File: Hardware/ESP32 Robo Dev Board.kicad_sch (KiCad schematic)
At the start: 19 parts, among them J1 PRG, U1 ESP32-S3-WROOM-1, U2 AMS1117-3.3, U5 TCA9548ARGER

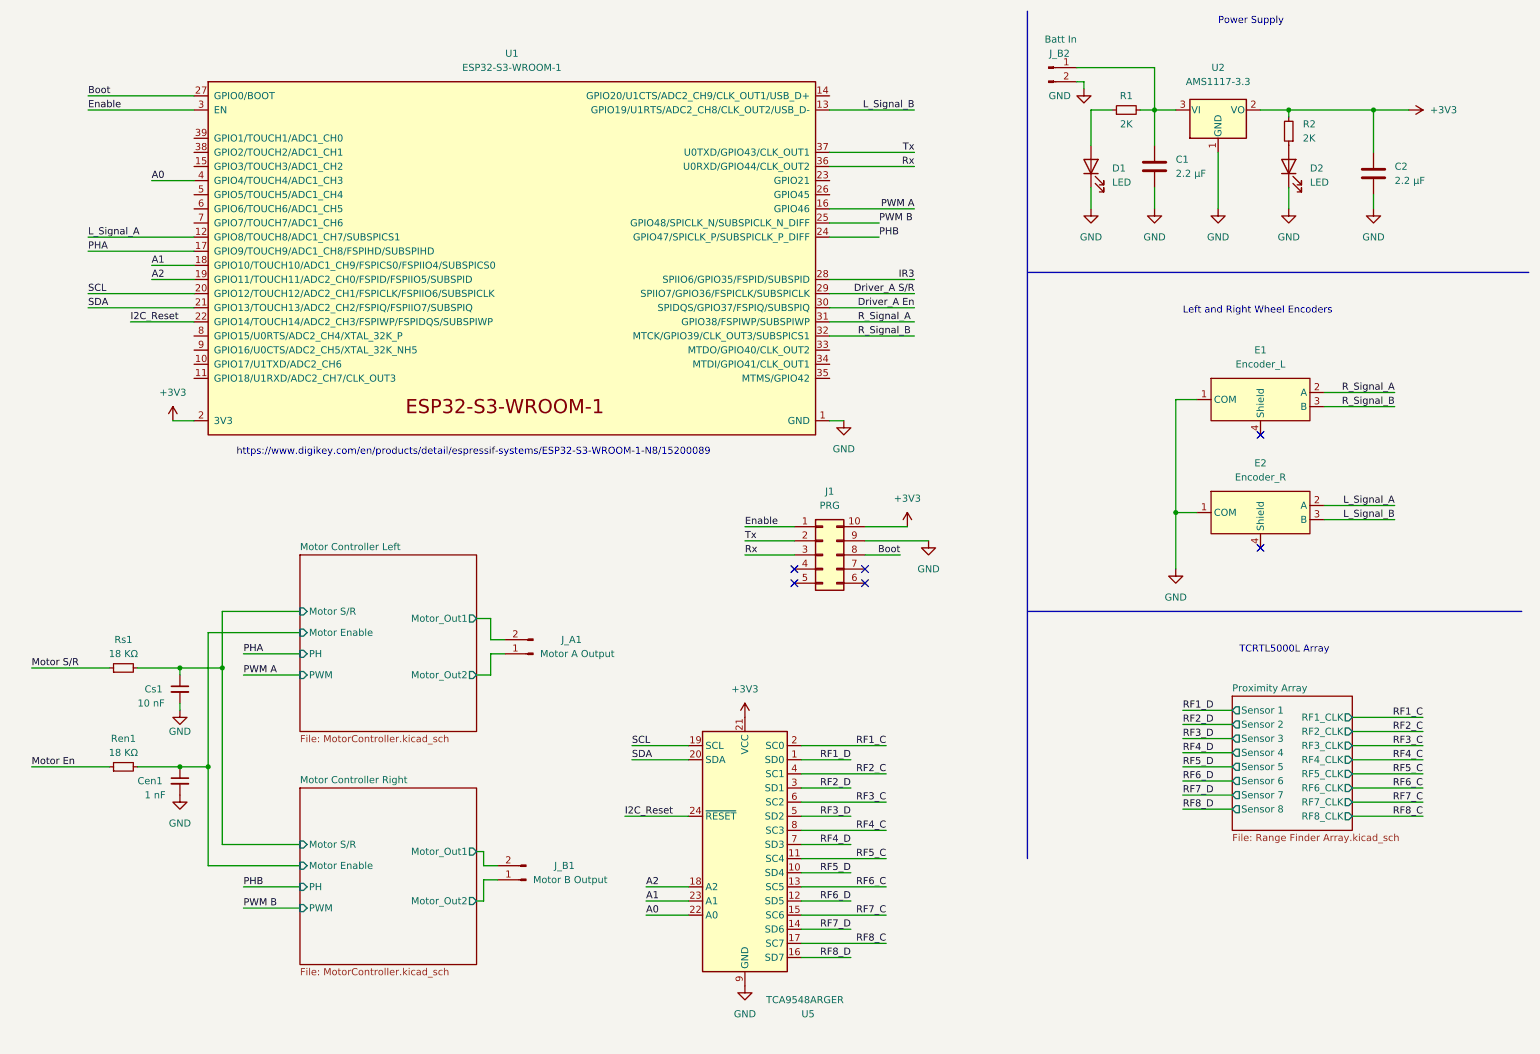
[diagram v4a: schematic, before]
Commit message: I2C Interface Established
Run Traces for all Sensors

Mark unused Pins

Sub-Optimally run said traces
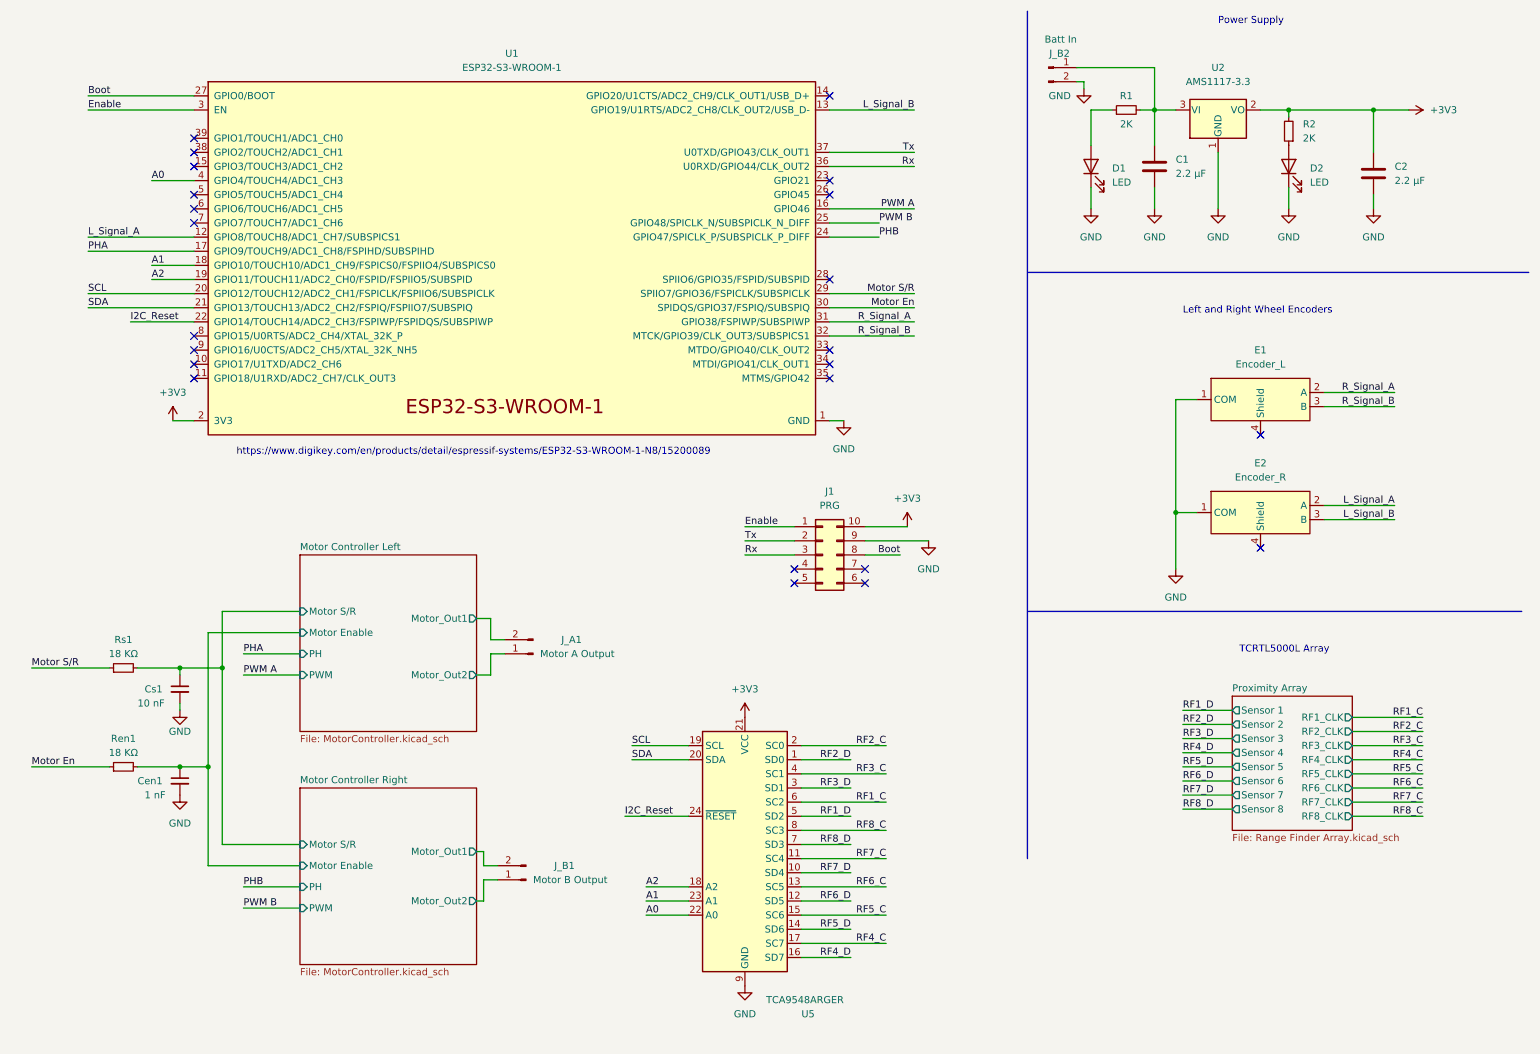
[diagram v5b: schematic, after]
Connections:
- net Driver_A En is gone; now on net Motor En: U1.30 (SPIDQS/GPIO37/FSPIQ/SUBSPIQ)
- net Driver_A S/R is gone; now on net Motor S/R: U1.29 (SPIIO7/GPIO36/FSPICLK/SUBSPICLK)
- net RF1_C: now also U5.6 (SC2); no longer U5.2 (SC0)
- net RF1_D: now also U5.5 (SD2); no longer U5.1 (SD0)
- net RF2_C: now also U5.2 (SC0); no longer U5.4 (SC1)
- net RF2_D: now also U5.1 (SD0); no longer U5.3 (SD1)
- net RF3_C: now also U5.4 (SC1); no longer U5.6 (SC2)
- net RF3_D: now also U5.3 (SD1); no longer U5.5 (SD2)
- net RF4_C: now also U5.17 (SC7); no longer U5.8 (SC3)
- net RF4_D: now also U5.16 (SD7); no longer U5.7 (SD3)
- net RF5_C: now also U5.15 (SC6); no longer U5.11 (SC4)
- net RF5_D: now also U5.14 (SD6); no longer U5.10 (SD4)
- net RF7_C: now also U5.11 (SC4); no longer U5.15 (SC6)
- net RF7_D: now also U5.10 (SD4); no longer U5.14 (SD6)
- net RF8_C: now also U5.8 (SC3); no longer U5.17 (SC7)
- net RF8_D: now also U5.7 (SD3); no longer U5.16 (SD7)
- net IR3: no longer names the net of U1.28 (SPIIO6/GPIO35/FSPID/SUBSPID)
- no-connect marks 6 -> 23

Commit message: Fix Thoughholes
Fixed Schematic Parity DRC issue.

Taught some standard practices by the Foxy Boy

Co-Authored-By: KenwoodFox <31870999+KenwoodFox@users.noreply.github.com>
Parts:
- added H1: (no value), symbol Mechanical:MountingHole_Pad
- added H2, H3, H4: MountingHole_Pad, MountingHole:MountingHole_2.2mm_M2_DIN965_Pad, symbol Mechanical:MountingHole_Pad
- renumbered U5 to U2, U2 to U3
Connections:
- net GND: now also H1.1, H2.1, H3.1, H4.1

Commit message: Add Throughholes
Added Through holes in a far better what than before.

Got advice from the Foxy Fellow

Co-Authored-By: KenwoodFox <31870999+KenwoodFox@users.noreply.github.com>
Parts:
- H1: value (none) -> MountingHole_Pad; footprint (none) -> MountingHole:MountingHole_2.2mm_M2_DIN965_Pad
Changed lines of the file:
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@@
     (title "TurtleBot Mainboard")
     (date "2022-11-27")
-    (rev "0.1")
+    (rev "${REVISION}")
     (company "Amoskeag Technologies")
+    (comment 4 "${FULL_REVISION}")
   )
   (junction (at 43.18 148.59) (diameter 0) (color 0 0 0 0)
@@
       (effects (font (size 1.27 1.27)) (justify left))
     )
-    (property "Value" "" (id 1) (at 17.78 189.2299 0)
+    (property "Value" "MountingHole_Pad" (id 1) (at 17.78 189.2299 0)
       (effects (font (size 1.27 1.27)) (justify left) hide)
     )
-    (property "Footprint" "" (id 2) (at 15.24 189.23 0)
+    (property "Footprint" "MountingHole:MountingHole_2.2mm_M2_DIN965_Pad" (id 2) (at 15.24 189.23 0)
       (effects (font (size 1.27 1.27)) hide)
     )
@@
   (symbol (lib_id "Graphic:Logo_Open_Hardware_Small") (at 261.62 175.26 0) (unit 1)
     (in_bom yes) (on_board yes) (fields_autoplaced)
-    (property "Reference" "#LOGO?" (id 0) (at 261.62 168.275 0)
-      (effects (font (size 1.27 1.27)) hide)
-    )
-    (property "Value" "" (id 1) (at 261.62 180.975 0)
-      (effects (font (size 1.27 1.27)) hide)
-    )
-    (property "Footprint" "" (id 2) (at 261.62 175.26 0)
+    (property "Reference" "#LOGO1" (id 0) (at 261.62 168.275 0)
+      (effects (font (size 1.27 1.27)) hide)
+    )
+    (property "Value" "Logo_Open_Hardware_Small" (id 1) (at 261.62 180.975 0)
+      (effects (font (size 1.27 1.27)) hide)
+    )
+    (property "Footprint" "Symbol:OSHW-Logo2_7.3x6mm_SilkScreen" (id 2) (at 261.62 175.26 0)
       (effects (font (size 1.27 1.27)) hide)
     )
@@
   (symbol (lib_id "Amoskeag-KiCAD-Lib:AT_Logo") (at 276.86 175.26 0) (unit 1)
     (in_bom yes) (on_board yes) (fields_autoplaced)
-    (property "Reference" "#G?" (id 0) (at 276.86 170.8713 0)
-      (effects (font (size 1.27 1.27)) hide)
-    )
-    (property "Value" "" (id 1) (at 276.86 179.6487 0)
+    (property "Reference" "#G1" (id 0) (at 276.86 170.8713 0)
+      (effects (font (size 1.27 1.27)) hide)
+    )
+    (property "Value" "AT_Logo" (id 1) (at 276.86 179.6487 0)
       (effects (font (size 1.27 1.27)) hide)
     )
@@
       (effects (font (size 1.27 1.27)) hide)
     )
-    (property "Value" "" (id 1) (at 15.24 196.85 0))
+    (property "Value" "GND" (id 1) (at 15.24 196.85 0))
     (property "Footprint" "" (id 2) (at 15.24 193.04 0)
       (effects (font (size 1.27 1.27)) hide)
@@
   (symbol_instances
     (path "/bc5273c3-012f-45b1-962a-d2f6bccb6a9a"
-      (reference "#G?") (unit 1) (value "AT_Logo") (footprint "")
+      (reference "#G1") (unit 1) (value "AT_Logo") (footprint "")
     )
     (path "/bbe411a0-2e88-4725-b110-84205d860b3c"
-      (reference "#LOGO?") (unit 1) (value "Logo_Open_Hardware_Small") (footprint "Symbol:OSHW-Logo2_7.3x6mm_SilkScreen")
+      (reference "#LOGO1") (unit 1) (value "Logo_Open_Hardware_Small") (footprint "Symbol:OSHW-Logo2_7.3x6mm_SilkScreen")
     )
     (path "/efc531b6-9e3c-46d2-a03c-acf3a17dc1eb"

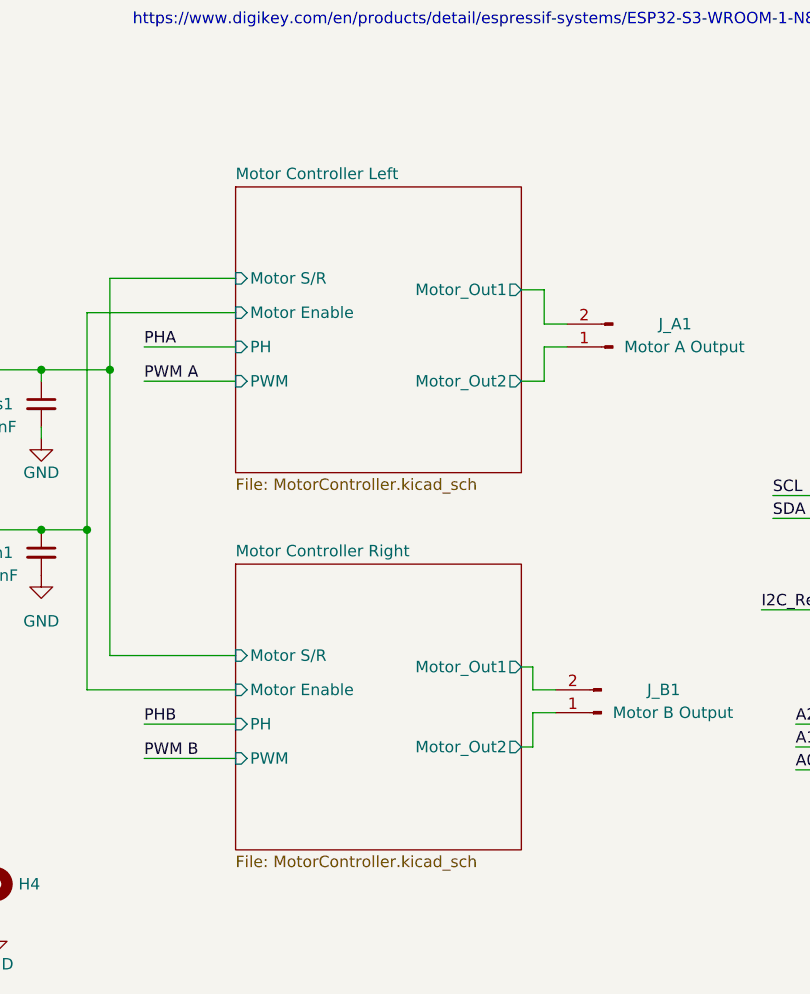
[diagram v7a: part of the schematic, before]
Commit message: Fixed Traces
Fix Traces that I messed up when I left college. Getting back to the project.
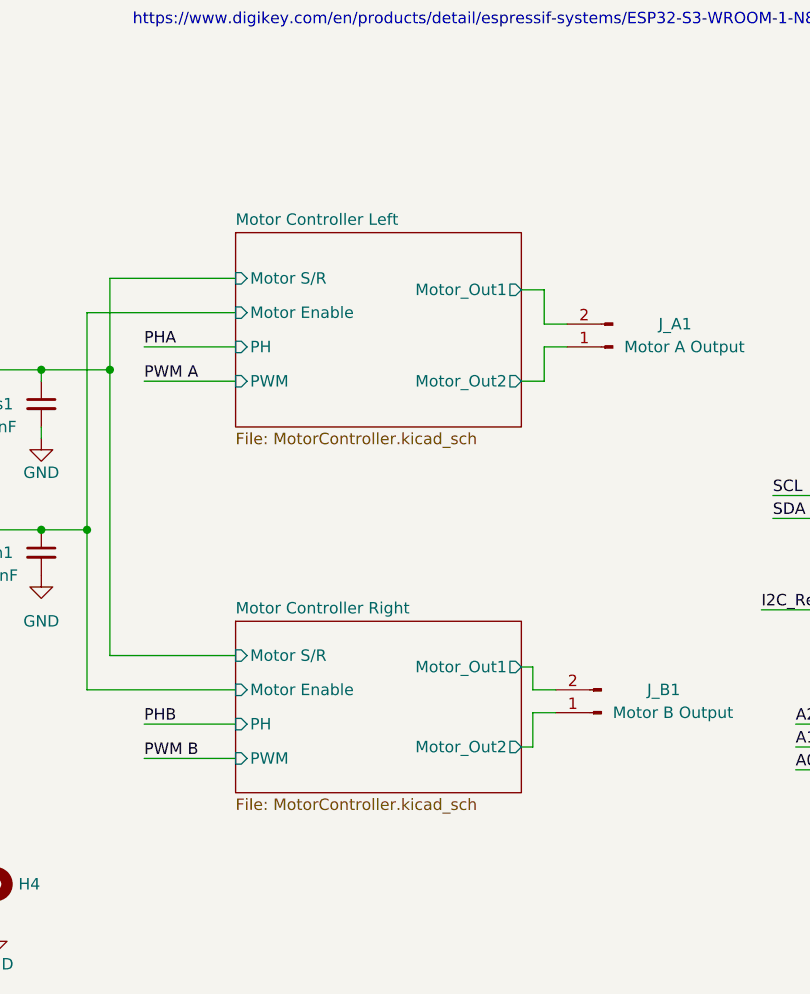
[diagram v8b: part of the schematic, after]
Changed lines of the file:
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@@
     (pin "1")
   )
-  (sheet (at 64.77 110.49) (size 31.75 31.75) (fields_autoplaced)
+  (sheet (at 64.77 115.57) (size 31.75 21.59) (fields_autoplaced)
     (stroke (width 0.1524) (type solid) (color 0 0 0 0))
     (fill (color 0 0 0 0.0000))
-    (property "Sheet name" "Motor Controller Left" (id 0) (at 64.77 109.7784 0)
+    (property "Sheet name" "Motor Controller Left" (id 0) (at 64.77 114.8584 0)
       (effects (font (size 1.27 1.27)) (justify left bottom))
     )
-    (property "Sheet file" "MotorController.kicad_sch" (id 1) (at 64.77 142.8246 0)
+    (property "Sheet file" "MotorController.kicad_sch" (id 1) (at 64.77 137.7446 0)
       (effects (font (size 1.27 1.27)) (justify left top))
     )
@@
     )
   )
-  (sheet (at 64.77 152.4) (size 31.75 31.75) (fields_autoplaced)
+  (sheet (at 64.77 158.75) (size 31.75 19.05) (fields_autoplaced)
     (stroke (width 0.1524) (type solid) (color 0 0 0 0))
     (fill (color 0 0 0 0.0000))
-    (property "Sheet name" "Motor Controller Right" (id 0) (at 64.77 151.6884 0)
+    (property "Sheet name" "Motor Controller Right" (id 0) (at 64.77 158.0384 0)
       (effects (font (size 1.27 1.27)) (justify left bottom))
     )
-    (property "Sheet file" "MotorController.kicad_sch" (id 1) (at 64.77 184.7346 0)
+    (property "Sheet file" "MotorController.kicad_sch" (id 1) (at 64.77 178.3846 0)
       (effects (font (size 1.27 1.27)) (justify left top))
     )
